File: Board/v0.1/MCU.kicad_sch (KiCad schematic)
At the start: 27 parts, among them J2 Conn_01x06_Male, SW1 RST_BTN, SW2 SCREEN_OFF_BTN, U1 ESP32-WROOM-32

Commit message: Clean schematics (add date and revision...)
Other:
- company: (none) -> Bzgec
- title: (none) -> MCU
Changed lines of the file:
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@@
 (kicad_sch (version 20211123) (generator eeschema)
   (paper "A4")
+  (title_block
+    (title "MCU")
+    (date "2022/01/06")
+    (rev "v0.1")
+    (company "Bzgec")
+  )
   (bus_alias "TOUCH_CONN" (members "SPI_MISO" "SPI_MOSI" "SPI_CLK" "SPI_CS" "IRQ"))
   (junction (at 33.02 22.86) (diameter 0) (color 0 0 0 0)
@@
   (symbol (lib_id "power:GND") (at 114.3 67.31 0) (unit 1)
     (in_bom yes) (on_board yes)
-    (property "Reference" "#PWR017" (id 0) (at 114.3 73.66 0)
+    (property "Reference" "#PWR016" (id 0) (at 114.3 73.66 0)
       (effects (font (size 1.27 1.27)) hide)
     )
@@
   (symbol (lib_id "power:+3.3V") (at 99.06 50.8 0) (unit 1)
     (in_bom yes) (on_board yes)
-    (property "Reference" "#PWR016" (id 0) (at 99.06 54.61 0)
+    (property "Reference" "#PWR015" (id 0) (at 99.06 54.61 0)
       (effects (font (size 1.27 1.27)) hide)
     )
@@
   (symbol (lib_id "power:+3.3V") (at 140.97 48.26 0) (unit 1)
     (in_bom yes) (on_board yes)
-    (property "Reference" "#PWR018" (id 0) (at 140.97 52.07 0)
+    (property "Reference" "#PWR017" (id 0) (at 140.97 52.07 0)
       (effects (font (size 1.27 1.27)) hide)
     )
@@
   (symbol (lib_id "power:GND") (at 140.97 128.27 0) (unit 1)
     (in_bom yes) (on_board yes)
-    (property "Reference" "#PWR019" (id 0) (at 140.97 134.62 0)
+    (property "Reference" "#PWR018" (id 0) (at 140.97 134.62 0)
       (effects (font (size 1.27 1.27)) hide)
     )
@@
   (symbol (lib_id "power:GND") (at 33.02 30.48 0) (unit 1)
     (in_bom yes) (on_board yes)
-    (property "Reference" "#PWR012" (id 0) (at 33.02 36.83 0)
+    (property "Reference" "#PWR011" (id 0) (at 33.02 36.83 0)
       (effects (font (size 1.27 1.27)) hide)
     )
@@
   (symbol (lib_id "power:+3.3V") (at 33.02 22.86 0) (unit 1)
     (in_bom yes) (on_board yes)
-    (property "Reference" "#PWR011" (id 0) (at 33.02 26.67 0)
+    (property "Reference" "#PWR010" (id 0) (at 33.02 26.67 0)
       (effects (font (size 1.27 1.27)) hide)
     )
@@
   (symbol (lib_id "power:GND") (at 25.4 181.61 0) (unit 1)
     (in_bom yes) (on_board yes)
-    (property "Reference" "#PWR010" (id 0) (at 25.4 187.96 0)
+    (property "Reference" "#PWR09" (id 0) (at 25.4 187.96 0)
       (effects (font (size 1.27 1.27)) hide)
     )
@@
   (symbol (lib_id "power:GND") (at 60.96 181.61 0) (unit 1)
     (in_bom yes) (on_board yes)
-    (property "Reference" "#PWR015" (id 0) (at 60.96 187.96 0)
+    (property "Reference" "#PWR014" (id 0) (at 60.96 187.96 0)
       (effects (font (size 1.27 1.27)) hide)
     )
@@
   (symbol (lib_id "power:+5V") (at 251.46 125.095 0) (unit 1)
     (in_bom yes) (on_board yes) (fields_autoplaced)
-    (property "Reference" "#PWR022" (id 0) (at 251.46 128.905 0)
+    (property "Reference" "#PWR021" (id 0) (at 251.46 128.905 0)
       (effects (font (size 1.27 1.27)) hide)
     )
@@
   (symbol (lib_id "power:GND") (at 238.76 137.795 270) (unit 1)
     (in_bom yes) (on_board yes) (fields_autoplaced)
-    (property "Reference" "#PWR021" (id 0) (at 232.41 137.795 0)
+    (property "Reference" "#PWR020" (id 0) (at 232.41 137.795 0)
       (effects (font (size 1.27 1.27)) hide)
     )
@@
   (symbol (lib_id "power:+3.3V") (at 60.96 160.02 0) (unit 1)
     (in_bom yes) (on_board yes) (fields_autoplaced)
-    (property "Reference" "#PWR014" (id 0) (at 60.96 163.83 0)
+    (property "Reference" "#PWR013" (id 0) (at 60.96 163.83 0)
       (effects (font (size 1.27 1.27)) hide)
     )
@@
   (symbol (lib_id "power:+3.3V") (at 38.1 107.95 0) (unit 1)
     (in_bom yes) (on_board yes) (fields_autoplaced)
-    (property "Reference" "#PWR013" (id 0) (at 38.1 111.76 0)
+    (property "Reference" "#PWR012" (id 0) (at 38.1 111.76 0)
       (effects (font (size 1.27 1.27)) hide)
     )
@@
   (symbol (lib_id "power:+3.3V") (at 231.14 125.095 0) (unit 1)
     (in_bom yes) (on_board yes) (fields_autoplaced)
-    (property "Reference" "#PWR020" (id 0) (at 231.14 128.905 0)
-      (effects (font (size 1.27 1.27)) hide)
-    )
+    (property "Reference" "#PWR019" (id 0) (at 231.14 128.905 0)
+      (effects (font (size 1.27 1.27)) hide)
+    )

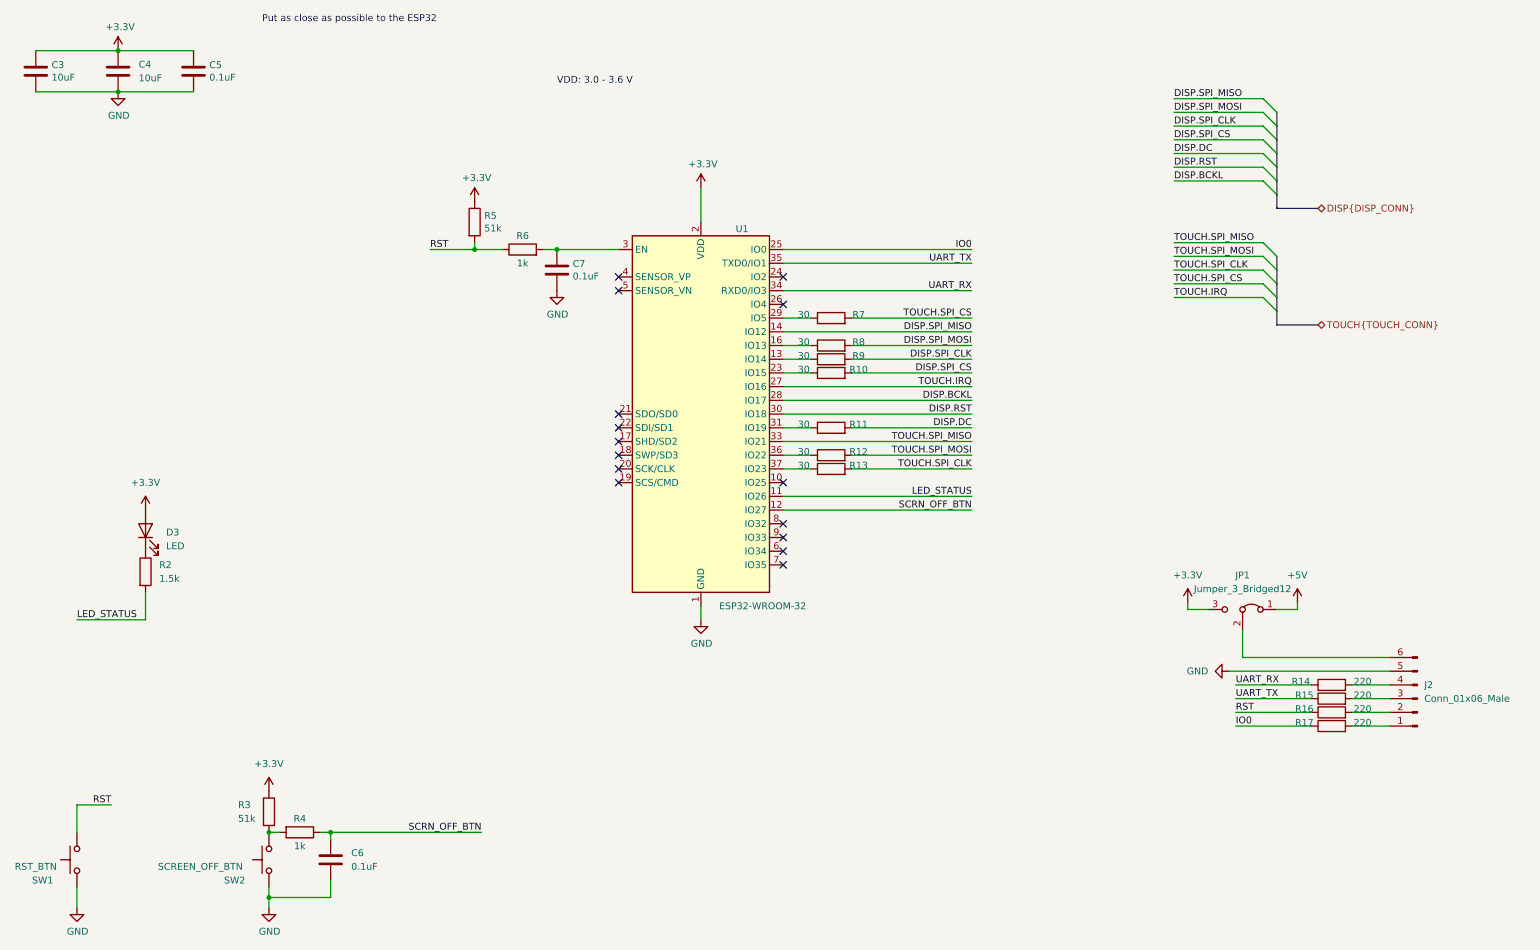
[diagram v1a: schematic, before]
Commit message: Add polyfuse, 3.3V status LED, USB_CONN sheet
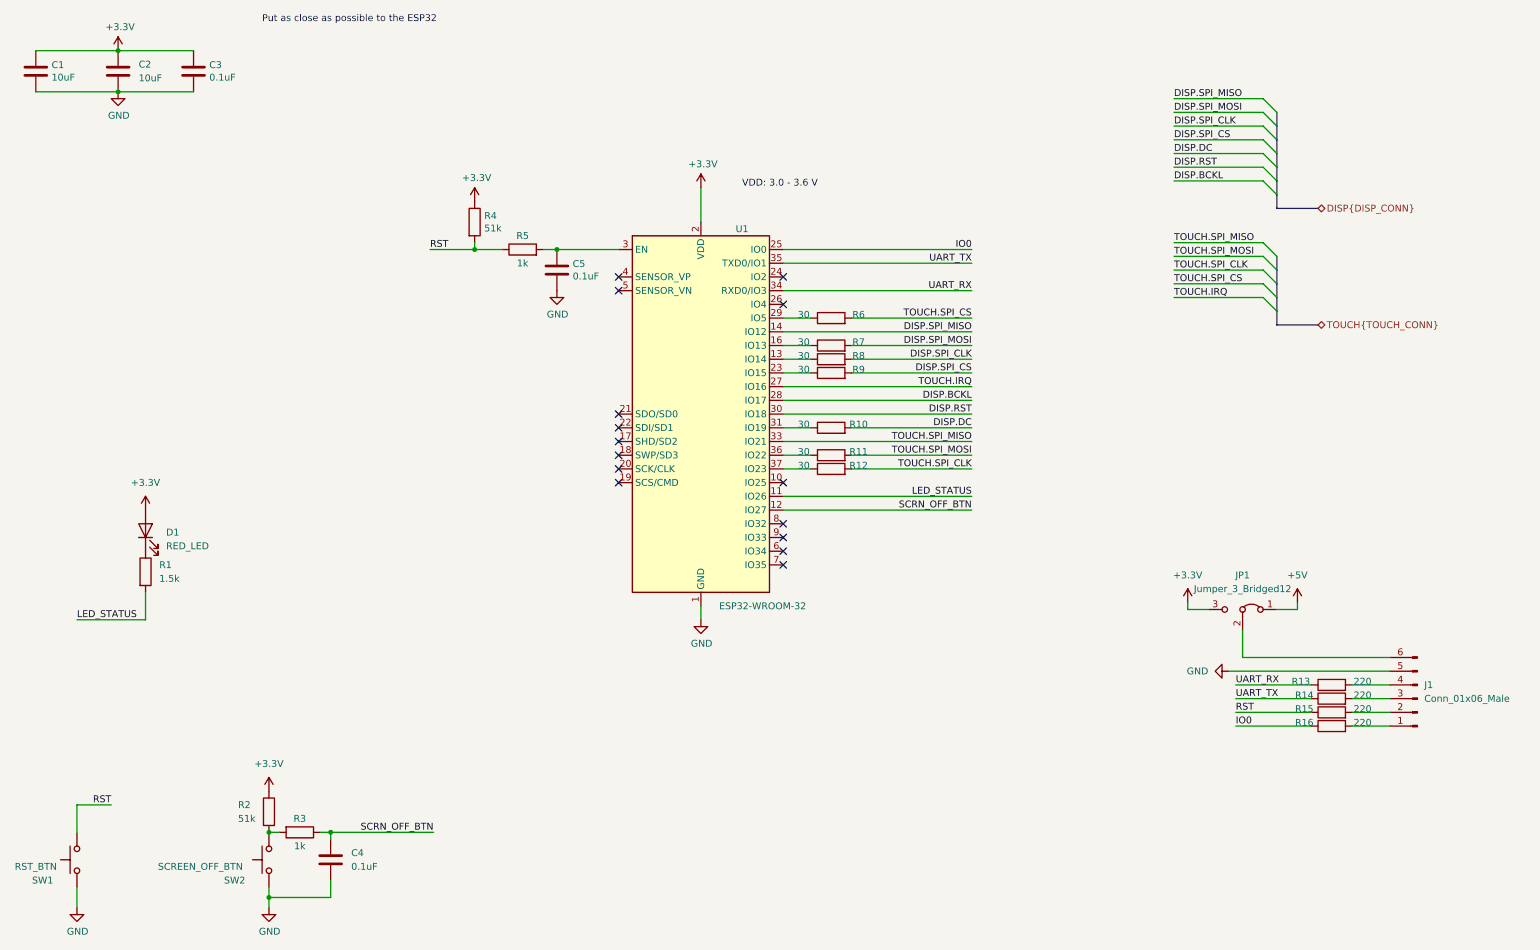
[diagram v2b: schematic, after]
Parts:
- D1: renamed from D3; value LED -> RED_LED
- renumbered C3 to C1, C4 to C2, C5 to C3, C6 to C4, C7 to C5, J2 to J1, R2 to R1, R11 to R10, R12 to R11, R13 to R12, R14 to R13, R15 to R14, R16 to R15, R17 to R16, R3 to R2, R4 to R3, R5 to R4, R6 to R5, R7 to R6, R8 to R7, R9 to R8, R10 to R9

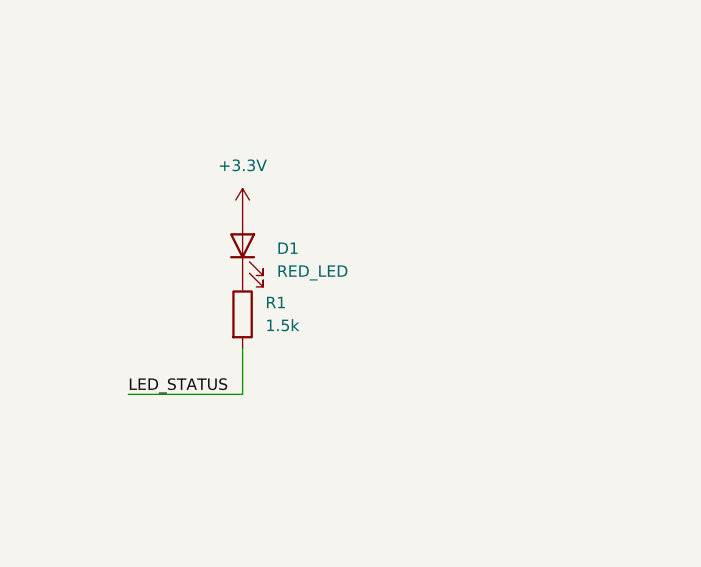
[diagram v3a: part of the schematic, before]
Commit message: Fix ILI9341 display symbol (pin numbering)
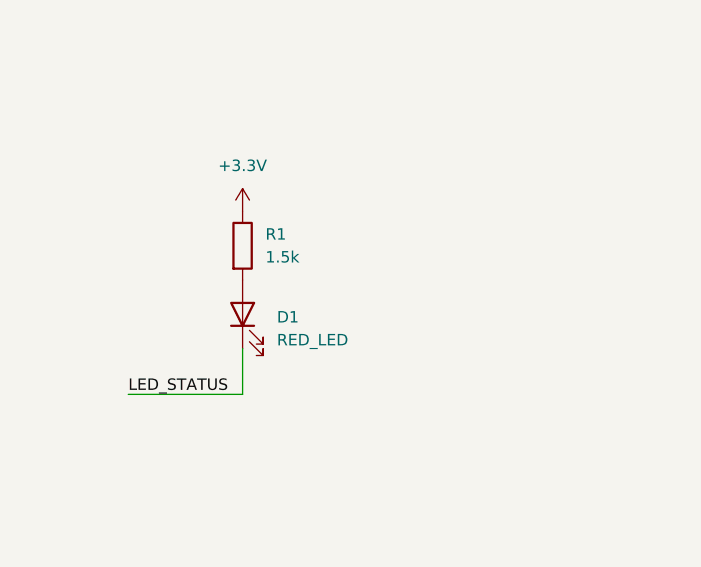
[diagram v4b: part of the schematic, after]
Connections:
- net +3V3: now also R1.1; no longer D1.2 (A)
- net LED_STATUS: now also D1.1 (K); no longer R1.2
- new net: D1.2 (A), R1.2
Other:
- moved on the sheet: D1, R1
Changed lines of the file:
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@@
     (pin "2")
   )
-  (symbol (lib_id "Device:LED") (at 38.1 111.76 90) (unit 1)
-    (in_bom yes) (on_board yes) (fields_autoplaced)
-    (property "Reference" "D1" (id 0) (at 41.91 112.0774 90)
-      (effects (font (size 1.27 1.27)) (justify right))
-    )
-    (property "Value" "RED_LED" (id 1) (at 41.91 114.6174 90)
-      (effects (font (size 1.27 1.27)) (justify right))
-    )
-    (property "Footprint" "Diode_SMD:D_0603_1608Metric_Pad1.05x0.95mm_HandSolder" (id 2) (at 38.1 111.76 0)
-      (effects (font (size 1.27 1.27)) hide)
-    )
-    (property "Datasheet" "https://www.we-online.com/katalog/datasheet/150060RS75000.pdf" (id 3) (at 38.1 111.76 0)
+  (symbol (lib_id "Device:LED") (at 38.1 119.38 90) (unit 1)
+    (in_bom yes) (on_board yes) (fields_autoplaced)
+    (property "Reference" "D1" (id 0) (at 41.91 119.6974 90)
+      (effects (font (size 1.27 1.27)) (justify right))
+    )
+    (property "Value" "RED_LED" (id 1) (at 41.91 122.2374 90)
+      (effects (font (size 1.27 1.27)) (justify right))
+    )
+    (property "Footprint" "Diode_SMD:D_0603_1608Metric_Pad1.05x0.95mm_HandSolder" (id 2) (at 38.1 119.38 0)
+      (effects (font (size 1.27 1.27)) hide)
+    )
+    (property "Datasheet" "https://www.we-online.com/katalog/datasheet/150060RS75000.pdf" (id 3) (at 38.1 119.38 0)
       (effects (font (size 1.27 1.27)) hide)
     )
@@
     (pin "2")
   )
-  (symbol (lib_id "Device:R") (at 38.1 119.38 0) (unit 1)
-    (in_bom yes) (on_board yes) (fields_autoplaced)
-    (property "Reference" "R1" (id 0) (at 40.64 118.1099 0)
-      (effects (font (size 1.27 1.27)) (justify left))
-    )
-    (property "Value" "1.5k" (id 1) (at 40.64 120.6499 0)
-      (effects (font (size 1.27 1.27)) (justify left))
-    )
-    (property "Footprint" "Resistor_SMD:R_0603_1608Metric_Pad0.98x0.95mm_HandSolder" (id 2) (at 36.322 119.38 90)
-      (effects (font (size 1.27 1.27)) hide)
-    )
-    (property "Datasheet" "~" (id 3) (at 38.1 119.38 0)
-      (effects (font (size 1.27 1.27)) hide)
-    )
+  (symbol (lib_id "Device:R") (at 38.1 111.76 0) (unit 1)
+    (in_bom yes) (on_board yes) (fields_autoplaced)
+    (property "Reference" "R1" (id 0) (at 40.64 110.4899 0)
+      (effects (font (size 1.27 1.27)) (justify left))
+    )
+    (property "Value" "1.5k" (id 1) (at 40.64 113.0299 0)
+      (effects (font (size 1.27 1.27)) (justify left))
+    )
+    (property "Footprint" "Resistor_SMD:R_0603_1608Metric_Pad0.98x0.95mm_HandSolder" (id 2) (at 36.322 111.76 90)
+      (effects (font (size 1.27 1.27)) hide)
+    )
+    (property "Datasheet" "~" (id 3) (at 38.1 111.76 0)
+      (effects (font (size 1.27 1.27)) hide)
+    )

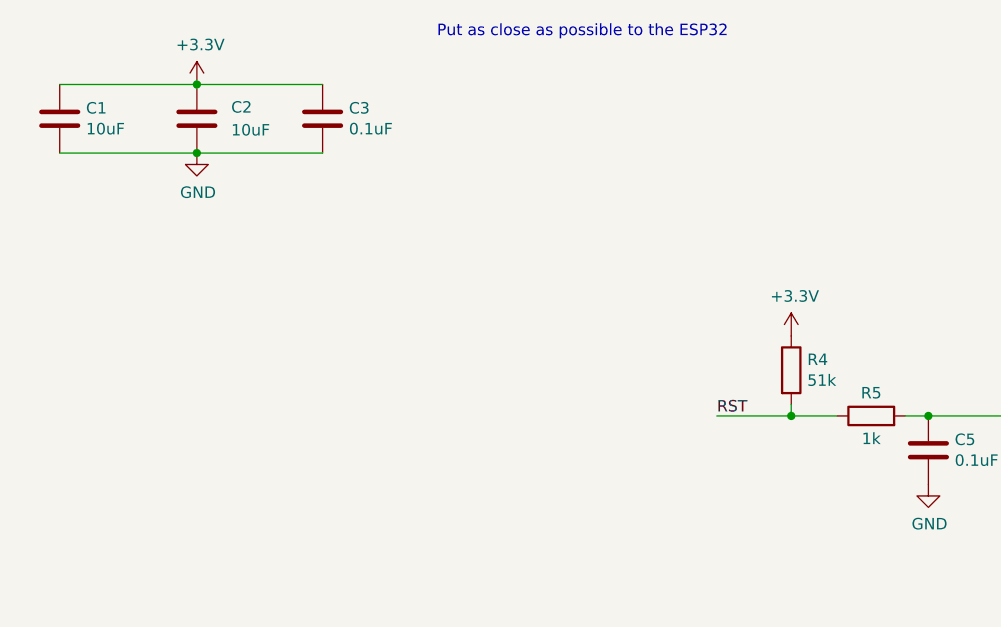
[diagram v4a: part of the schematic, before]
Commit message: Add info about ESP32 strapping pins
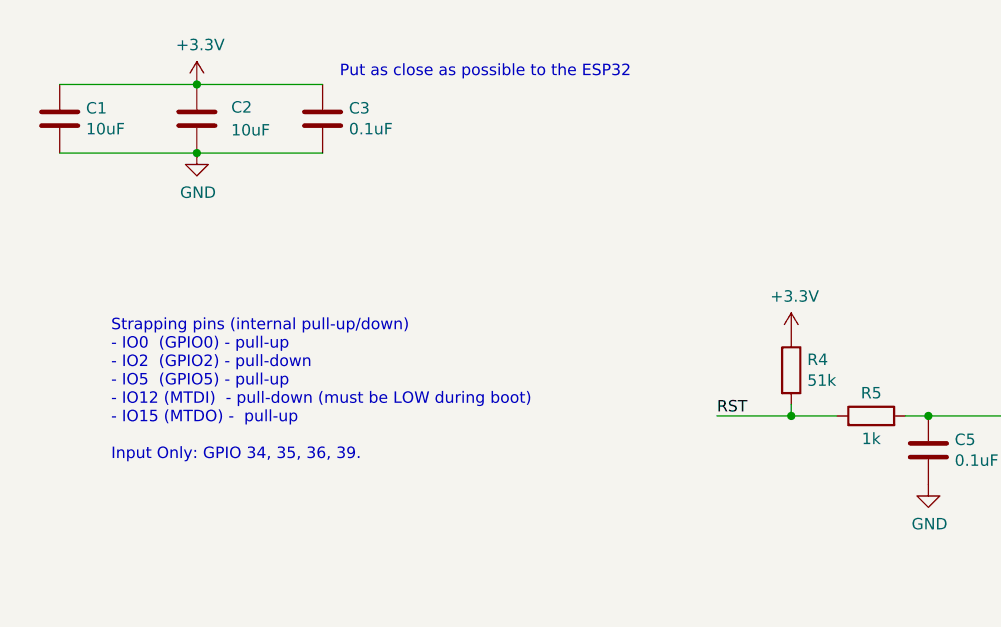
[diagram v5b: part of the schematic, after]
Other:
- note added: "Strapping pins (internal pull-up/down) - IO0 (GPIO0) - pull-up - IO2 (GPIO2) - pull-down - IO5 (GPIO5) - pull-up - IO12 (MTDI) - pull-down (must be LOW during boot) - IO15 (MTDO) - pull-up Input Only: GPIO 34, 35, 36, 39."
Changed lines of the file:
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@@
   (no_connect (at 156.21 118.11))
   (no_connect (at 125.73 67.31))
+  (no_connect (at 156.21 113.03))
   (no_connect (at 125.73 100.33))
   (no_connect (at 156.21 64.77))
-  (no_connect (at 156.21 110.49))
   (no_connect (at 156.21 102.87))
+  (no_connect (at 156.21 69.85))
   (no_connect (at 125.73 90.17))
   (no_connect (at 125.73 64.77))
-  (no_connect (at 156.21 69.85))
   (no_connect (at 125.73 92.71))
+  (no_connect (at 156.21 110.49))
   (no_connect (at 125.73 102.87))
-  (no_connect (at 156.21 113.03))
   (bus_entry (at 245.11 60.96) (size 2.54 2.54)
     (stroke (width 0) (type default) (color 0 0 0 0))
@@
     (stroke (width 0) (type default) (color 0 0 0 0))
   )
-  (text "Put as close as possible to the ESP32" (at 59.69 17.78 0)
+  (text "Put as close as possible to the ESP32" (at 48.895 22.225 0)
     (effects (font (size 1.27 1.27)) (justify left bottom))
   )
+  (text "Strapping pins (internal pull-up/down)\n- IO0  (GPIO0) - pull-up\n- IO2  (GPIO2) - pull-down\n- IO5  (GPIO5) - pull-up\n- IO12 (MTDI)  - pull-down (must be LOW during boot)\n- IO15 (MTDO) -  pull-up\n\nInput Only: GPIO 34, 35, 36, 39."
+    (at 23.495 64.77 0)
+    (effects (font (size 1.27 1.27)) (justify left bottom))
+  )
